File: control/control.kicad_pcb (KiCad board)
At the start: 2 copper layers, 50.3 x 43.1 mm, 53 parts, among them J1 Conn_01x02_Pin, J2 Conn_01x04_Male, J3 Conn_01x02_Pin, J4 Conn_01x07_Pin, P1 Conn_01x03_Pin, P2 Conn_01x03_Pin, P3 Conn_01x03_Pin, P4 Conn_01x03_Pin, SW2 SW_Push, U1 STM32F103C8Tx, Y1 8Mhz

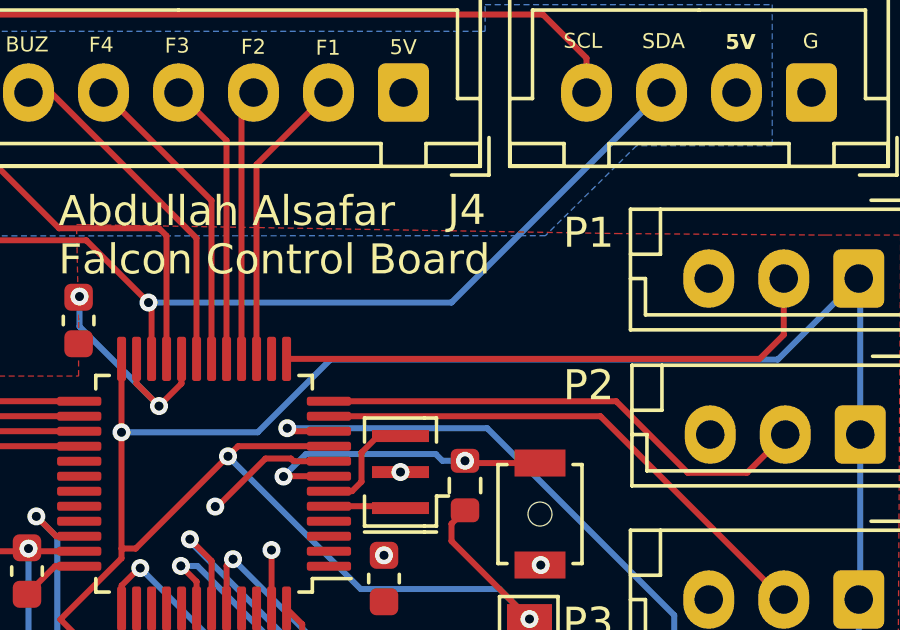
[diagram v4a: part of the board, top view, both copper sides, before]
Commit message: Touchups to revised control board
- Removed redundant battery connection in schematic
- Added labels to programming signals in schematic
- Added "Rev. ##" label on board
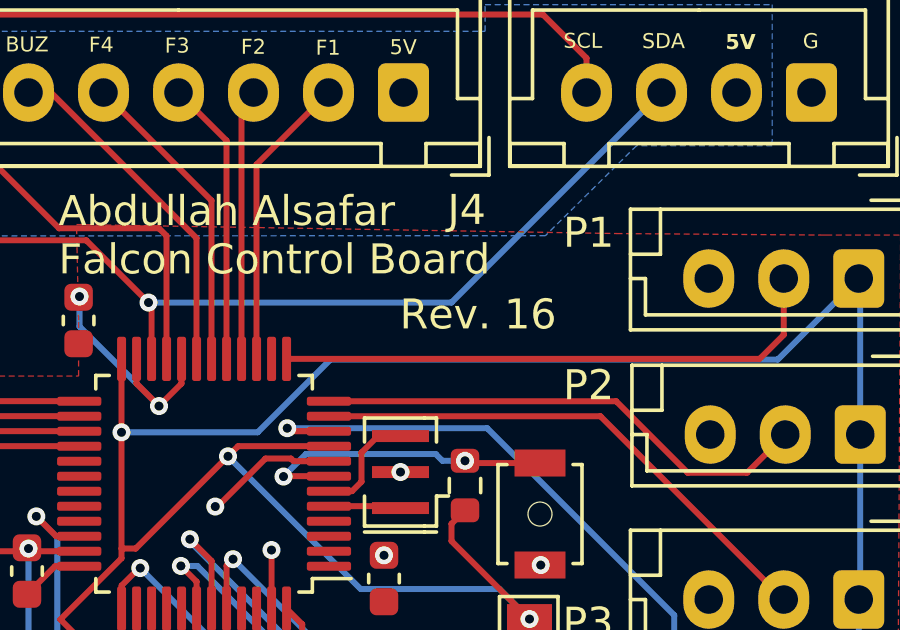
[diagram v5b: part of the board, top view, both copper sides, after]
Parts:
- renumbered REF** to H**
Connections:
- net SWCLK renamed /SWCLK
- net SWDIO renamed /SWDIO
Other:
- board text added: "Rev. ${REVISION}"
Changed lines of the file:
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@@
   (title_block
     (title "Falcon Control MAIN")
-    (date "2023-11-30")
-    (rev "15")
+    (date "2024-02-15")
+    (rev "16")
     (company "Human Powered Vehicles Design Team @ UOFT")
     (comment 1 "Supervised by Savo Bajic")
@@
   (net 49 "unconnected-(U1-PB8-Pad45)")
   (net 50 "unconnected-(U1-PA15-Pad38)")
-  (net 51 "SWCLK")
-  (net 52 "SWDIO")
+  (net 51 "/SWDIO")
+  (net 52 "/SWCLK")
   (footprint "Connector_JST:JST_EH_B3B-EH-A_1x03_P2.50mm_Vertical" (layer "F.Cu")
     (at 123.975 77.25 180)
@@
     (descr "Mounting Hole 3.2mm, no annular, M3")
     (tags "mounting hole 3.2mm no annular m3")
-    (attr exclude_from_pos_files exclude_from_bom)
-    (fp_text reference "REF**" (at 0 -4.2) (layer "F.SilkS") hide
+    (attr board_only exclude_from_pos_files exclude_from_bom)
+    (fp_text reference "H**" (at 0 -4.2) (layer "F.SilkS") hide
         (effects (font (size 1 1) (thickness 0.15)))
     )
@@
       (net 3 "+3.3V") (pinfunction "Pin_1") (pintype "passive"))
     (pad "2" thru_hole oval (at 0 2.54) (size 1.7 1.7) (drill 1) (layers "*.Cu" "*.Mask")
-      (net 51 "SWCLK") (pinfunction "Pin_2") (pintype "passive"))
+      (net 52 "/SWCLK") (pinfunction "Pin_2") (pintype "passive"))
     (pad "3" thru_hole oval (at 0 5.08) (size 1.7 1.7) (drill 1) (layers "*.Cu" "*.Mask")
-      (net 52 "SWDIO") (pinfunction "Pin_3") (pintype "passive"))
+      (net 51 "/SWDIO") (pinfunction "Pin_3") (pintype "passive"))
     (pad "4" thru_hole oval (at 0 7.62) (size 1.7 1.7) (drill 1) (layers "*.Cu" "*.Mask")
       (net 1 "GND") (pinfunction "Pin_4") (pintype "passive"))
@@
       (net 43 "unconnected-(U1-PA12-Pad33)") (pinfunction "PA12") (pintype "bidirectional+no_connect"))
     (pad "34" smd roundrect (at 4.1625 -1.75 180) (size 1.475 0.3) (layers "F.Cu" "F.Paste" "F.Mask") (roundrect_rratio 0.25)
-      (net 52 "SWDIO") (pinfunction "PA13") (pintype "bidirectional"))
+      (net 51 "/SWDIO") (pinfunction "PA13") (pintype "bidirectional"))
     (pad "35" smd roundrect (at 4.1625 -2.25 180) (size 1.475 0.3) (layers "F.Cu" "F.Paste" "F.Mask") (roundrect_rratio 0.25)
       (net 1 "GND") (pinfunction "VSS") (pintype "passive"))
@@
       (net 3 "+3.3V") (pinfunction "VDD") (pintype "power_in"))
     (pad "37" smd roundrect (at 2.75 -4.1625 180) (size 0.3 1.475) (layers "F.Cu" "F.Paste" "F.Mask") (roundrect_rratio 0.25)
-      (net 51 "SWCLK") (pinfunction "PA14") (pintype "bidirectional"))
+      (net 52 "/SWCLK") (pinfunction "PA14") (pintype "bidirectional"))
     (pad "38" smd roundrect (at 2.25 -4.1625 180) (size 0.3 1.475) (layers "F.Cu" "F.Paste" "F.Mask") (roundrect_rratio 0.25)
       (net 50 "unconnected-(U1-PA15-Pad38)") (pinfunction "PA15") (pintype "bidirectional+no_connect"))
@@
     (descr "Mounting Hole 3.2mm, no annular, M3")
     (tags "mounting hole 3.2mm no annular m3")
-    (attr exclude_from_pos_files exclude_from_bom)
-    (fp_text reference "REF**" (at 0 -4.2) (layer "F.SilkS") hide
+    (attr board_only exclude_from_pos_files exclude_from_bom)
+    (fp_text reference "H**" (at 0 -4.2) (layer "F.SilkS") hide
         (effects (font (size 1 1) (thickness 0.15)))
     )
@@
     (effects (font (size 1 1) (thickness 0.2) bold) (justify left bottom mirror))
   )
+  (gr_text "Rev. ${REVISION}" (at 152.6 68) (layer "F.SilkS")
+    (effects (font (size 1 1) (thickness 0.15)) (justify right))
+  )
   (gr_text "SCL" (at 157.79 91.16) (layer "F.SilkS")
     (effects (font (size 0.5 0.5) (thickness 0.1)) (justify left bottom))
@@
   (segment (start 163.15 89.238654) (end 163.15 90.191346) (width 0.2) (layer "B.Cu") (net 48))
   (segment (start 161.523654 90.865) (end 159.258654 93.13) (width 0.2) (layer "B.Cu") (net 48))
-  (segment (start 138.725 76.45) (end 138.68717 76.45) (width 0.2) (layer "F.Cu") (net 51))
-  (segment (start 138.68717 76.45) (end 138.1025 77.03467) (width 0.2) (layer "F.Cu") (net 51))
-  (segment (start 138.1025 77.03467) (end 138.1025 77.8025) (width 0.2) (layer "F.Cu") (net 51))
-  (via (at 138.725 76.45) (size 0.6) (drill 0.3) (layers "F.Cu" "B.Cu") (net 51))
-  (segment (start 153.225 89.690686) (end 155.434314 91.9) (width 0.2) (layer "B.Cu") (net 51))
-  (segment (start 138.725 76.45) (end 141.325 79.05) (width 0.2) (layer "B.Cu") (net 51))
-  (segment (start 142.6 79.05) (end 153.225 89.675) (width 0.2) (layer "B.Cu") (net 51))
-  (segment (start 153.225 89.675) (end 153.225 89.690686) (width 0.2) (layer "B.Cu") (net 51))
-  (segment (start 141.325 79.05) (end 142.6 79.05) (width 0.2) (layer "B.Cu") (net 51))
-  (segment (start 158.975 91.9) (end 161.16 89.715) (width 0.2) (layer "B.Cu") (net 51))
-  (segment (start 155.434314 91.9) (end 158.975 91.9) (width 0.2) (layer "B.Cu") (net 51))
-  (segment (start 161.16 89.715) (end 162 89.715) (width 0.2) (layer "B.Cu") (net 51))
-  (segment (start 135.26 74.72783) (end 135.92217 75.39) (width 0.2) (layer "F.Cu") (net 52))
-  (segment (start 135.92217 75.39) (end 136.69 75.39) (width 0.2) (layer "F.Cu") (net 52))
-  (via (at 135.26 74.72783) (size 0.6) (drill 0.3) (layers "F.Cu" "B.Cu") (net 52))
-  (segment (start 142.25 79.75) (end 152.379657 89.879657) (width 0.2) (layer "B.Cu") (net 52))
-  (segment (start 135.96 80.88) (end 136.73 81.65) (width 0.2) (layer "B.Cu") (net 52))
-  (segment (start 136.73 81.65) (end 139.5 81.65) (width 0.2) (layer "B.Cu") (net 52))
-  (segment (start 139.5 81.65) (end 141.4 79.75) (width 0.2) (layer "B.Cu") (net 52))
-  (segment (start 154.429214 94.39) (end 159.865 94.39) (width 0.2) (layer "B.Cu") (net 52))
-  (segment (start 159.865 94.39) (end 162 92.255) (width 0.2) (layer "B.Cu") (net 52))
-  (segment (start 152.379657 92.340443) (end 154.429214 94.39) (width 0.2) (layer "B.Cu") (net 52))
-  (segment (start 152.379657 89.879657) (end 152.379657 92.340443) (width 0.2) (layer "B.Cu") (net 52))
-  (segment (start 135.26 74.72783) (end 135.96 75.42783) (width 0.2) (layer "B.Cu") (net 52))
-  (segment (start 135.96 75.42783) (end 135.96 80.88) (width 0.2) (layer "B.Cu") (net 52))
-  (segment (start 141.4 79.75) (end 142.25 79.75) (width 0.2) (layer "B.Cu") (net 52))
+  (segment (start 135.26 74.72783) (end 135.92217 75.39) (width 0.2) (layer "F.Cu") (net 51))
+  (segment (start 135.92217 75.39) (end 136.69 75.39) (width 0.2) (layer "F.Cu") (net 51))
+  (via (at 135.26 74.72783) (size 0.6) (drill 0.3) (layers "F.Cu" "B.Cu") (net 51))
+  (segment (start 142.25 79.75) (end 152.379657 89.879657) (width 0.2) (layer "B.Cu") (net 51))
+  (segment (start 135.96 80.88) (end 136.73 81.65) (width 0.2) (layer "B.Cu") (net 51))
+  (segment (start 136.73 81.65) (end 139.5 81.65) (width 0.2) (layer "B.Cu") (net 51))
+  (segment (start 139.5 81.65) (end 141.4 79.75) (width 0.2) (layer "B.Cu") (net 51))
+  (segment (start 154.429214 94.39) (end 159.865 94.39) (width 0.2) (layer "B.Cu") (net 51))
+  (segment (start 159.865 94.39) (end 162 92.255) (width 0.2) (layer "B.Cu") (net 51))
+  (segment (start 152.379657 92.340443) (end 154.429214 94.39) (width 0.2) (layer "B.Cu") (net 51))
+  (segment (start 152.379657 89.879657) (end 152.379657 92.340443) (width 0.2) (layer "B.Cu") (net 51))
+  (segment (start 135.26 74.72783) (end 135.96 75.42783) (width 0.2) (layer "B.Cu") (net 51))
+  (segment (start 135.96 75.42783) (end 135.96 80.88) (width 0.2) (layer "B.Cu") (net 51))
+  (segment (start 141.4 79.75) (end 142.25 79.75) (width 0.2) (layer "B.Cu") (net 51))
+  (segment (start 138.725 76.45) (end 138.68717 76.45) (width 0.2) (layer "F.Cu") (net 52))
+  (segment (start 138.68717 76.45) (end 138.1025 77.03467) (width 0.2) (layer "F.Cu") (net 52))
+  (segment (start 138.1025 77.03467) (end 138.1025 77.8025) (width 0.2) (layer "F.Cu") (net 52))
+  (via (at 138.725 76.45) (size 0.6) (drill 0.3) (layers "F.Cu" "B.Cu") (net 52))
+  (segment (start 153.225 89.690686) (end 155.434314 91.9) (width 0.2) (layer "B.Cu") (net 52))
+  (segment (start 138.725 76.45) (end 141.325 79.05) (width 0.2) (layer "B.Cu") (net 52))
+  (segment (start 142.6 79.05) (end 153.225 89.675) (width 0.2) (layer "B.Cu") (net 52))
+  (segment (start 153.225 89.675) (end 153.225 89.690686) (width 0.2) (layer "B.Cu") (net 52))
+  (segment (start 141.325 79.05) (end 142.6 79.05) (width 0.2) (layer "B.Cu") (net 52))
+  (segment (start 158.975 91.9) (end 161.16 89.715) (width 0.2) (layer "B.Cu") (net 52))
+  (segment (start 155.434314 91.9) (end 158.975 91.9) (width 0.2) (layer "B.Cu") (net 52))
+  (segment (start 161.16 89.715) (end 162 89.715) (width 0.2) (layer "B.Cu") (net 52))
   (zone (net 3) (net_name "+3.3V") (layer "F.Cu") (hatch edge 0.5)
     (priority 1)

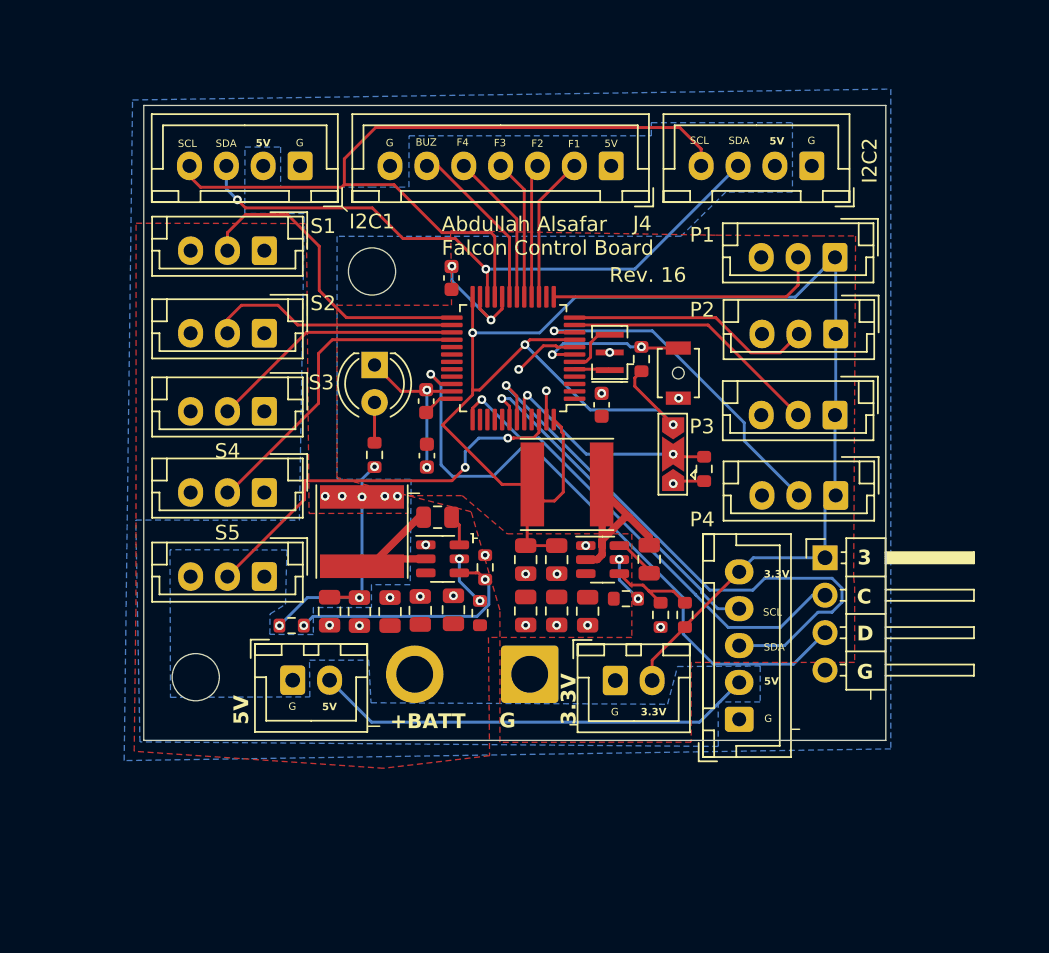
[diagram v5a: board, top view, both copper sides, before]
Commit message: increased size and updated silkscreen labels
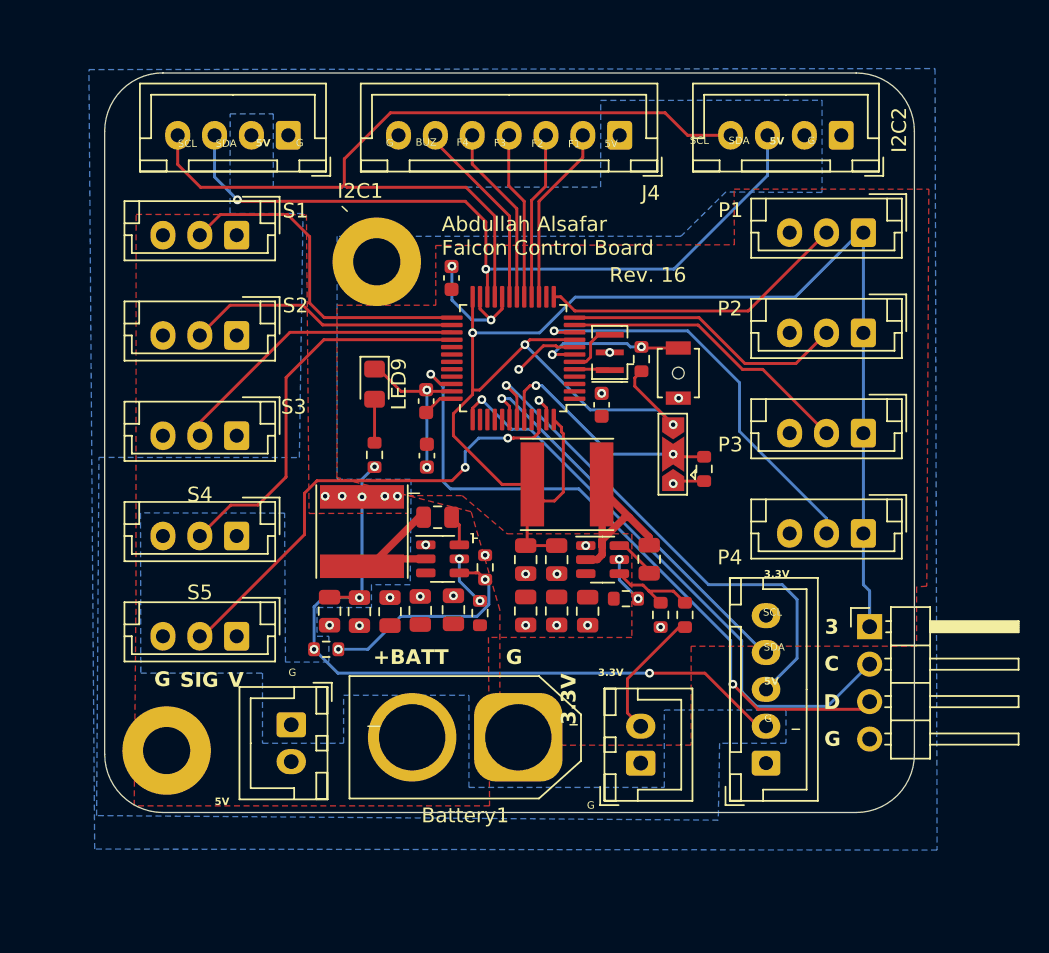
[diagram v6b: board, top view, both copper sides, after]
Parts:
- Battery1: footprint Connector_Wire:SolderWire-2sqmm_1x02_P7.8mm_D2mm_OD3.9mm -> Connector_AMASS:AMASS_XT60-F_1x02_P7.20mm_Vertical
- LED9: footprint LED_THT:LED_D4.0mm -> LED_SMD:LED_0805_2012Metric_Pad1.15x1.40mm_HandSolder
- moved J1 5.86 mm to (149.5, 101.1), turned to 90 degrees
- moved J2 5.57 mm to (165.0, 91.8)
- moved H** 5.35 mm to (117.3, 100.2)
- moved S5 4.46 mm to (122.1, 92.5)
- moved Battery1 4.34 mm to (141.2, 99.3)
- moved S4 3.50 mm to (122.1, 85.7)
- moved ISC3 3.48 mm to (158.0, 101.1)
- moved P4 3.19 mm to (164.6, 85.5)
- moved J3 3.03 mm to (125.8, 98.5), turned to -90 degrees
- moved I2C2 2.88 mm to (163.1, 58.5)
- moved R9 2.84 mm to (128.2, 93.4)
- moved P1 2.55 mm to (164.6, 65.1)
- moved S3 2.50 mm to (122.1, 78.9)
- moved P3 2.28 mm to (164.6, 78.7)
- moved I2C1 2.22 mm to (125.6, 58.5)
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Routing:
- net SDA_{TOCTRL}: track 43.3 -> 52.1 mm
- net /SWCLK: track 32.2 -> 39.8 mm
- net SDA_{TOMAIN}: track 41.0 -> 35.3 mm
- net SER4: track 21.5 -> 26.6 mm
- net POT4: track 23.4 -> 28.1 mm
- net SCL_{TOCTRL}: track 55.9 -> 60.4 mm
- net SER5: track 27.4 -> 31.9 mm
- net SER3: track 17.4 -> 20.5 mm
- net SCL_{TOMAIN}: track 23.7 -> 26.7 mm
- net /SWDIO: track 43.7 -> 46.5 mm, vias 1 -> 2
- net +5V: track 47.6 -> 50.4 mm, vias 8 -> 9
- net POT2: track 16.7 -> 19.2 mm
- net POT3: track 17.7 -> 20.1 mm
- net LED_{FIELD1}: track 9.87 -> 12.2 mm
- net POT1: track 18.8 -> 21.1 mm
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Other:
- board size 50.3 x 43.1 mm -> 54.9 x 50.2 mm
- board text added: "SIG"
- board text added: "V"

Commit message: updated board shape, added silkscreen labels & new LEDs
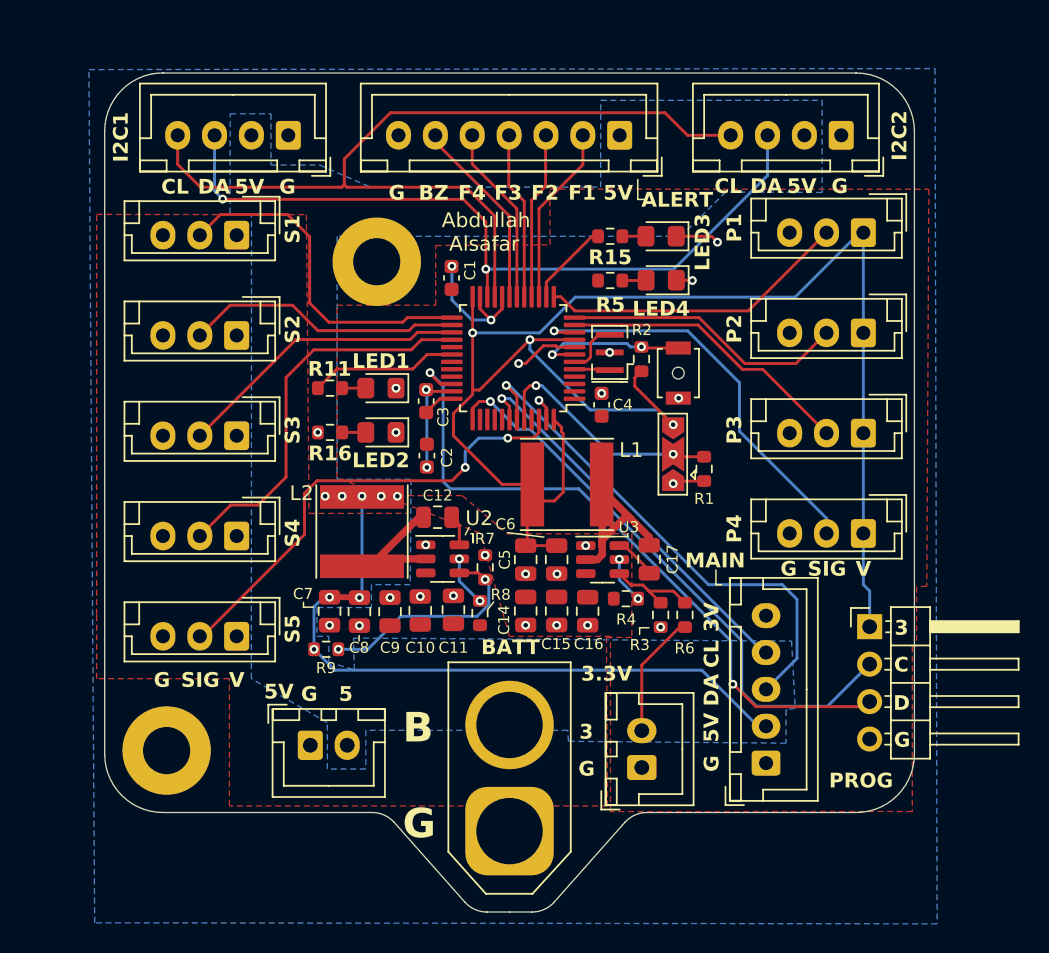
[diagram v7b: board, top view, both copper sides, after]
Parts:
- added G***: LOGO, Symbol:HPVDT-Logo_1526.1x139.6mm_SilkScreen, B.Cu at (140.2, 81.4)
- added G***: LOGO, Symbol:PCBWAY-Logo_23.7x23.7mm_SilkScreen, B.Cu at (147.5, 68.3)
- added LED1: LED1, LED_SMD:LED_0805_2012Metric_Pad1.15x1.40mm_HandSolder, F.Cu at (131.9, 75.7)
- added LED2: LED1, LED_SMD:LED_0805_2012Metric_Pad1.15x1.40mm_HandSolder, F.Cu at (131.9, 78.7)
- added LED3: LED1, LED_SMD:LED_0805_2012Metric_Pad1.15x1.40mm_HandSolder, F.Cu at (150.9, 65.4)
- added R11: 420, Resistor_SMD:R_0603_1608Metric, F.Cu at (128.4, 75.7)
- added R15: 420, Resistor_SMD:R_0603_1608Metric, F.Cu at (147.4, 65.4)
- added R16: 420, Resistor_SMD:R_0603_1608Metric, F.Cu at (128.4, 78.7)
- added REF**: KiCad-Logo2_5mm_SilkScreen, Symbol:KiCad-Logo2_5mm_SilkScreen, B.Cu at (132.8, 73.7)
- moved LED4 20.7 mm to (150.9, 68.4), turned to 180 degrees
- moved R5 19.9 mm to (147.4, 68.4), turned to 180 degrees
- moved Battery1 6.39 mm to (140.6, 105.7), turned to 90 degrees
- moved J3 1.90 mm to (127.1, 99.9), turned to 0 degrees
- moved J1 0.31 mm to (149.6, 101.4)
- renumbered J4 to ALERT, LED9 to LED4
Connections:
- R5 pad 2: +5V -> +3.3V
- U1 pad 14: unconnected-(U1-PA4-Pad14) -> LED3
- U1 pad 30: unconnected-(U1-PA9-Pad30) -> LED1
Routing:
- net LED1: track 0.00 -> 10.0 mm
- net LED3: track 0.00 -> 5.79 mm
- net +5V: track 50.4 -> 48.6 mm
- net Net-(LED3-A): track 0.00 -> 1.60 mm
- net Net-(LED1-A): track 0.00 -> 1.60 mm
- net Net-(LED2-A): track 0.00 -> 1.59 mm
- net Net-(LED4-A): track 2.95 -> 1.62 mm
- net SDA_{TOCTRL}: track 52.1 -> 52.6 mm
- net SER3: track 20.5 -> 20.0 mm
- net GND: track 28.7 -> 28.3 mm, vias 24 -> 28
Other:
- board size 54.9 x 50.2 mm -> 54.9 x 56.9 mm
- board text added: "3V"
- board text added: "5"
- board text added: "ALERT"
- board text added: "Abdullah"
- board text added: "Alsafar"
- board text added: "B"
- board text added: "BATT"
- board text added: "BZ"
- board text added: "CL"
- board text added: "Control Board"
- board text added: "DA"
- board text added: "Falcon"
- board text added: "I2C1"
- board text added: "I2C2"
- board text added: "MAIN"
- board text added: "P1"
- board text added: "P2"
- board text added: "P3"
- board text added: "P4"
- board text added: "PROG"
- board text added: "S1"
- board text added: "S2"
- board text added: "S3"
- board text added: "S4"
- board text added: "S5"
- board text removed: "+BATT"
- board text removed: "Abdullah Alsafar Falcon Control Board"
- board text removed: "BUZ"
- board text removed: "SCL"
- board text removed: "SDA"
